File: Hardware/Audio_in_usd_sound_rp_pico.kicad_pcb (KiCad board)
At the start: 2 copper layers, 100 x 100 mm, 275 parts, among them J1 ADC IN, J11 SDR ANT, J12 SDR Out, J13 ANT_BNC, J14 ANT_BNC, J15 Audio IN, J16 Audio IN, J17 Mini-jack socket, J4 Conn_02x20_Counter_Clockwise, J5 Conn_01x20, J6 Conn_01x20, J7 Conn_02x20_Counter_Clockwise, J8 BNC, Q1 MMBT2222A 1P, Q2 MMBT2222A 1P, Q3 MMBT2222A, SW1 Left, SW2 Right, T1 Screw Terminal, 4Px5.08mm, 20A, T2 Screw Terminal, 4Px5.08mm, 20A, U1 LSM6DSO32TR, U10 Si4732, U11 HS96L03W2C03, U12 L298N, U13 LM393DR2G, U15 DS18B20A10T6, U17 LM2937xS, U2 PCM1808PWR, U3 Pico, U4 MS5351M, U5 CJ431, U6 TSOP4438, U7 PI5C3253CQEX, U8 OPA1612AxD, U9 LM358, X1 Q13FC1350000400, Y1 X322525MSB4SI

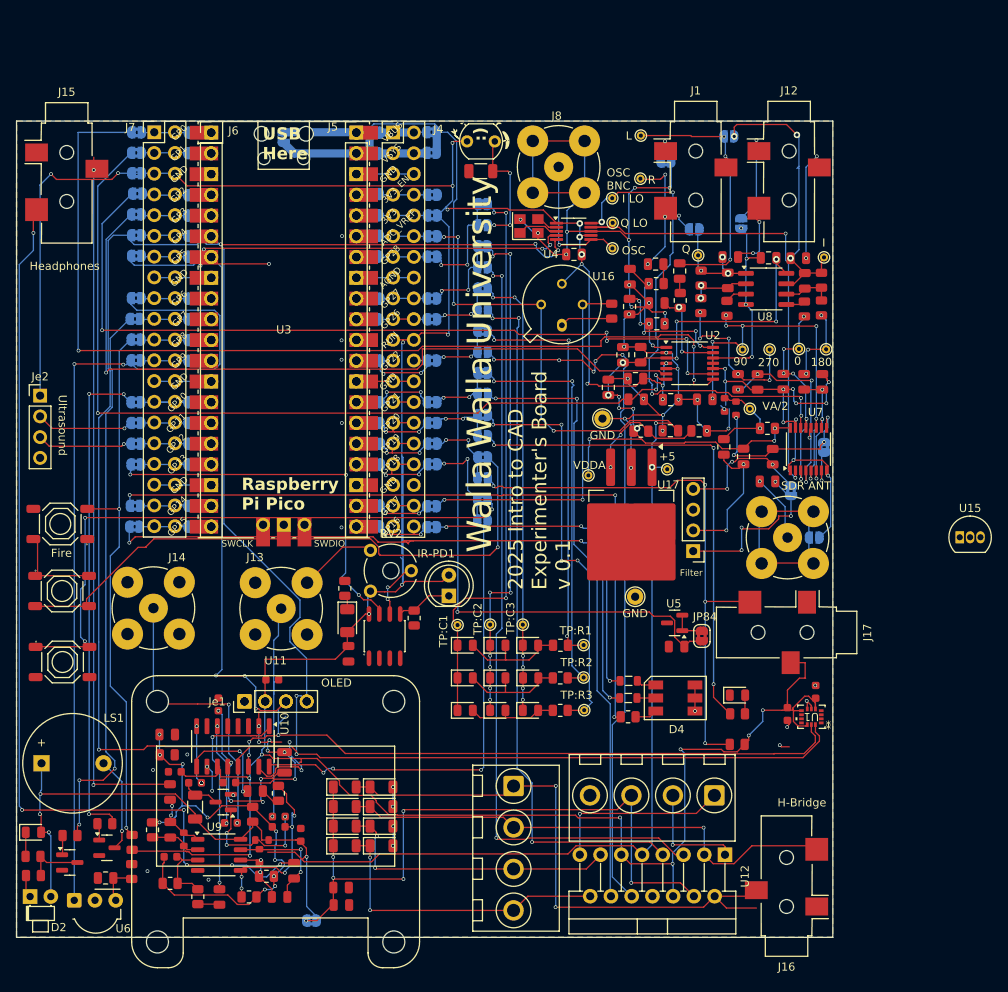
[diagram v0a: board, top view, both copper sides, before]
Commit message: Corrected the order of the Si4732 pinout in the schematic and removed the label indicating an incorrect order. I also rerouted the traces to those pins.
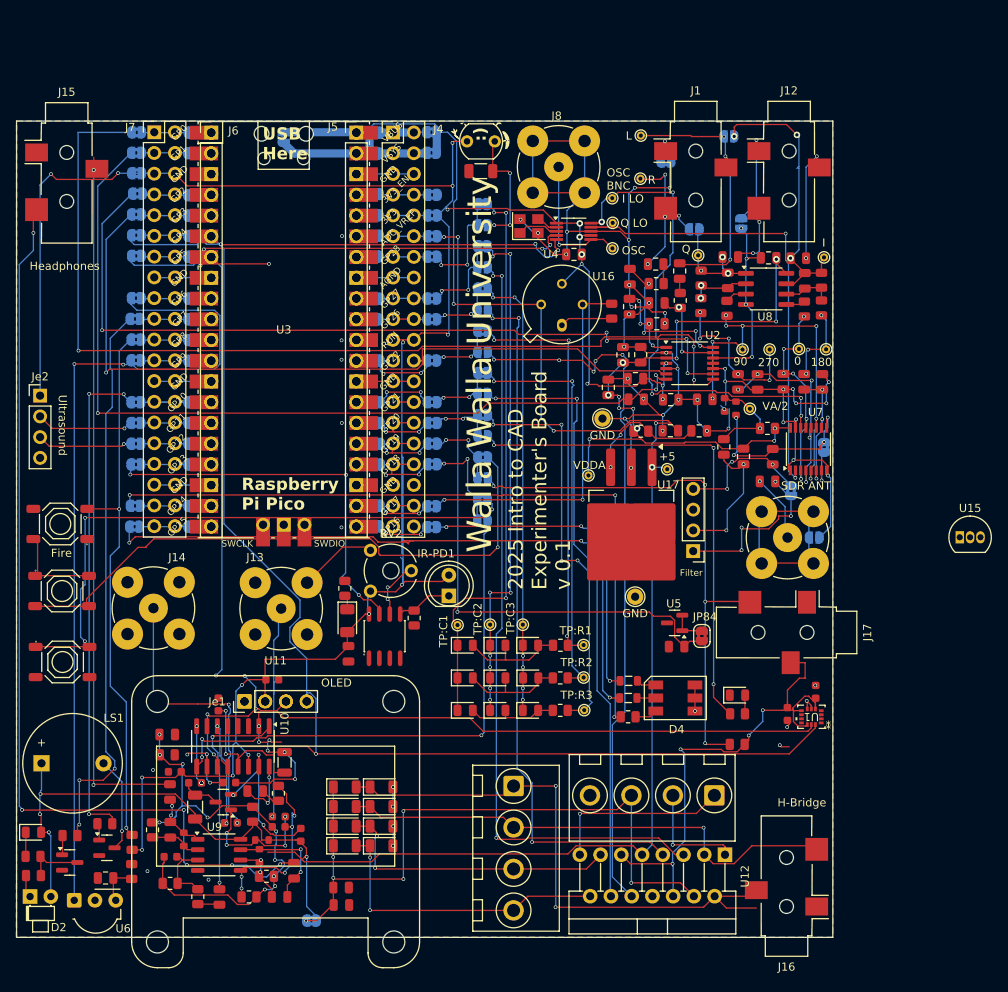
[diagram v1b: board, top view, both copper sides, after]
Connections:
- net <NO NET> renamed ~
- U10 pad 11: +3.3V -> /SCL
- U10 pad 12: Net-(U10-RCLK) -> /SDA
- U10 pad 13: /SDA -> Net-(U10-RCLK)
- U10 pad 14: /SCL -> +3.3V
- U10 pad 16: /~{RST} -> Net-(U10-ROUT)
- U10 pad 9: Net-(U10-ROUT) -> /~{RST}
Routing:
- net /SDA: track 292.2 -> 207.8 mm, vias 6 -> 4
- net +3.3V: track 415.0 -> 357.3 mm, vias 25 -> 26
- net GND: track 334.1 -> 351.2 mm
- net /~{RST}: track 57.6 -> 65.0 mm
- net Net-(U10-ROUT): track 12.3 -> 7.62 mm
- net Net-(U10-RCLK): track 23.2 -> 18.6 mm, vias 5 -> 2
- net /SCL: track 214.3 -> 212.2 mm, vias 11 -> 10
